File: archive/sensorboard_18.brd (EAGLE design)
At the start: 100 x 58 mm, 107 parts, among them IC1 ECMF02-2AMX6, IC2_ESP32S2WROOMM22S2 ESP32-S2-WROOM_M22S2H3200PH3Q0, IC4 TPA6211A1DRBR, J4_USB USB_CONN, J5_AUDIO SJ-3523-SMT-TR, J6_OAT 2.5mm JACK, J7 30310-6002HB, U1 LPS22HB, U10-MAG_SENSOR MMC5983MA, U11 LDL212PV33R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

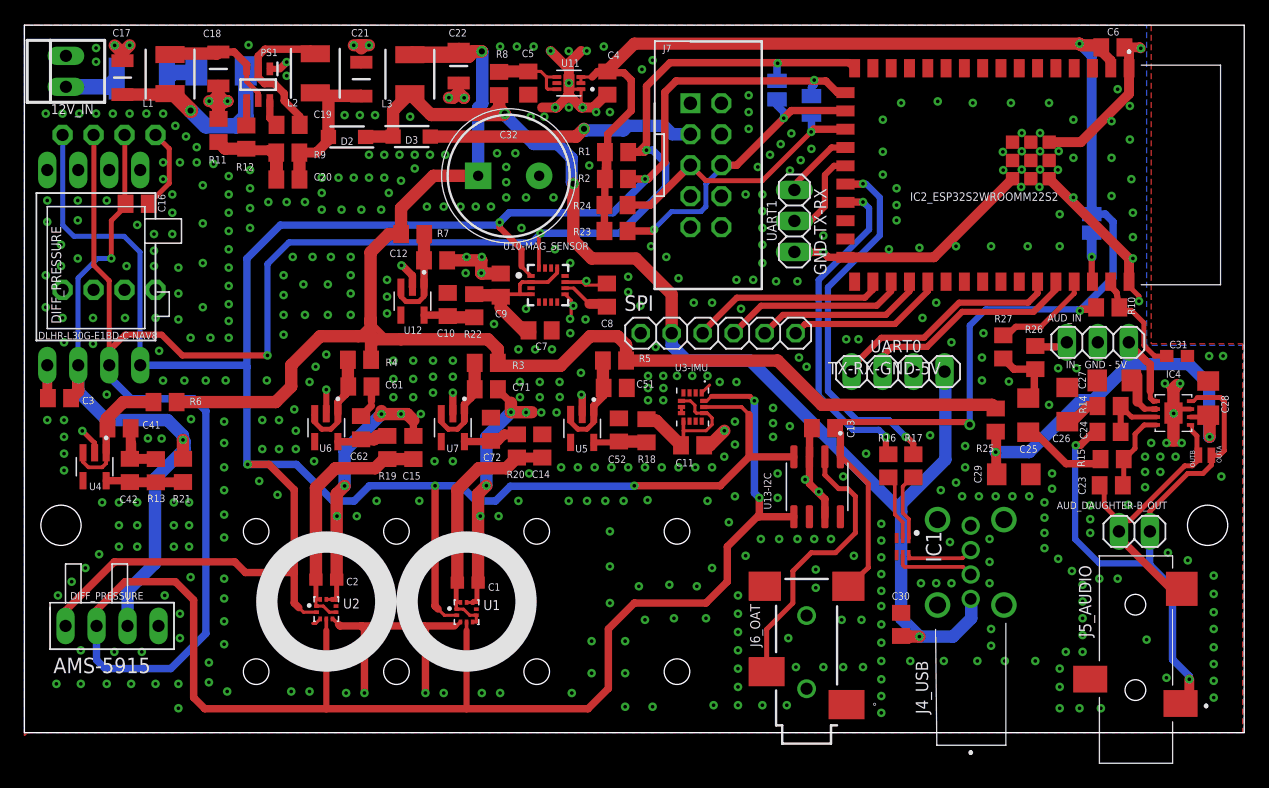
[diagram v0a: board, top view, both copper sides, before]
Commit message: Archive v18 files
Create archive directory with v18 files for use as assembly reference for previous board revision
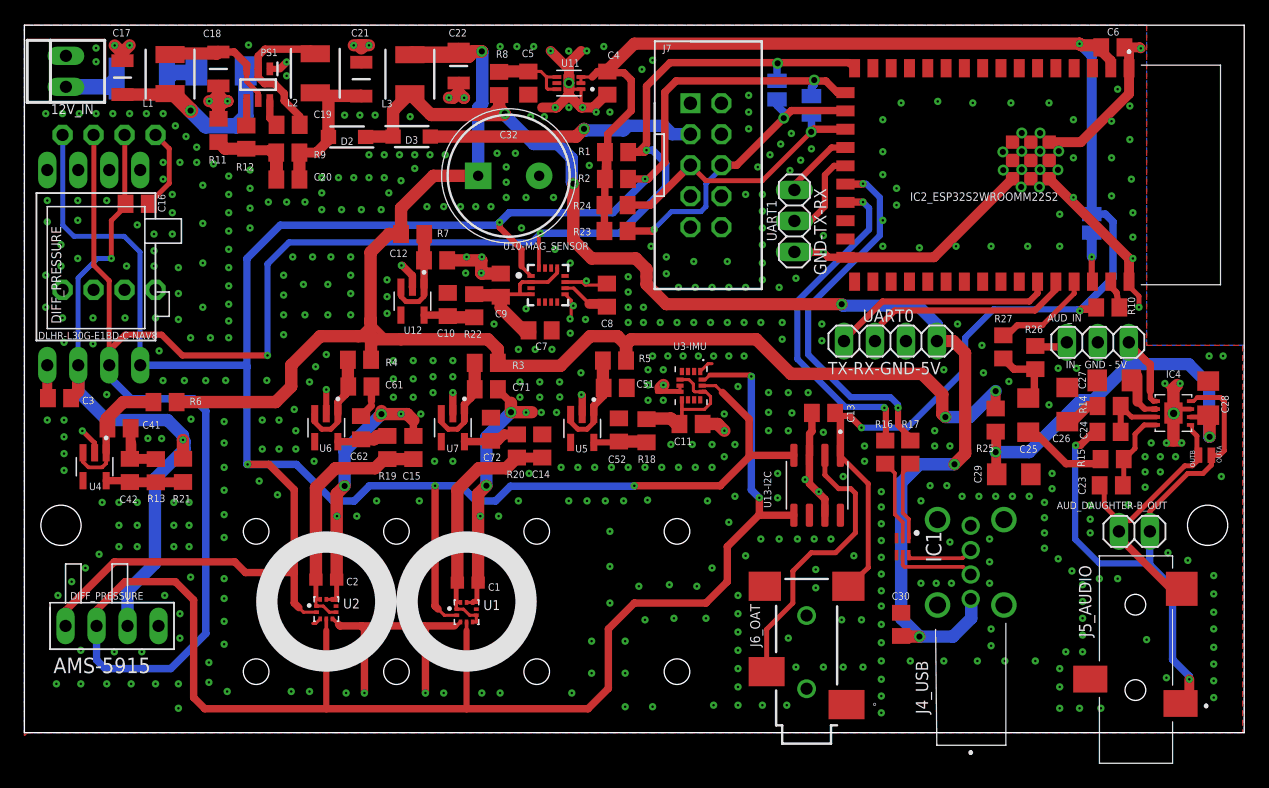
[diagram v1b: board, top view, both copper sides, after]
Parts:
- removed C31: 100nF, rcl:C0603
- removed SPI: (no value), pinhead_dD:1X06
- moved UART0 2.58 mm to (71.0, 32.1)
- moved C11 1.75 mm to (54.7, 25.3)
- moved U3-IMU 1.75 mm to (54.7, 28.4)
- moved C13 1.25 mm to (65.5, 26.2)
- moved R16 1.15 mm to (70.6, 23.0)
- moved R17 1.15 mm to (72.6, 23.0)
- moved U13-I2C 0.12 mm to (65.0, 20.3)
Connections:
- removed net FSPICLK: IC2_ESP32S2WROOMM22S2.30, SPI.5
- removed net FSPICS0: IC2_ESP32S2WROOMM22S2.28, SPI.3
- removed net FSPID_MOSI: IC2_ESP32S2WROOMM22S2.29, SPI.4
- removed net FSPIQ_MISO: IC2_ESP32S2WROOMM22S2.31, SPI.6
- net 5VD: no longer SPI.2
- net GND: no longer C31.2, SPI.1
- net N$7: no longer C31.1
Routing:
- net FSPICS0: track 16.2 -> 0.00 mm
- net FSPID_MOSI: track 15.1 -> 0.00 mm
- net FSPICLK: track 14.1 -> 0.00 mm
- net FSPIQ_MISO: track 13.0 -> 0.00 mm
- net N$7: track 8.95 -> 2.33 mm
- net 5VC: track 125.2 -> 131.0 mm, vias 1 -> 3
- net GND: track 207.2 -> 211.3 mm, vias 554 -> 578
- net 5VD: track 110.2 -> 112.9 mm, vias 3 -> 5
- net SDA0: track 261.9 -> 263.6 mm
- net 3V3_DIG: track 135.9 -> 134.3 mm
- net N$28: track 5.46 -> 6.69 mm
- net N$27: track 5.63 -> 6.57 mm
- net USB_D+: track 27.7 -> 28.6 mm
- net VDD3F: track 12.3 -> 11.6 mm
- net SCL0: track 223.0 -> 223.7 mm
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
